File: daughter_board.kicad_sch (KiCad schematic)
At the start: 8 parts

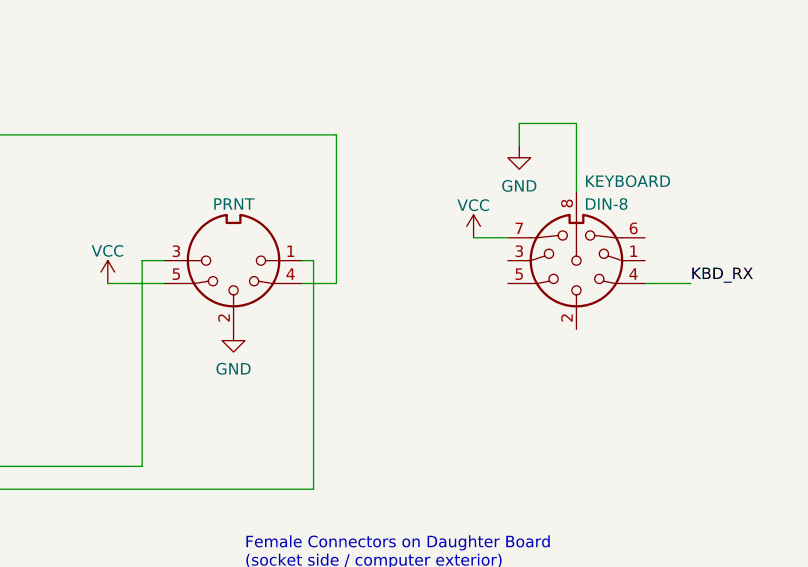
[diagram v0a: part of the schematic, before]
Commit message: Some changes, unfortunately merged with upgrade to kicad v7
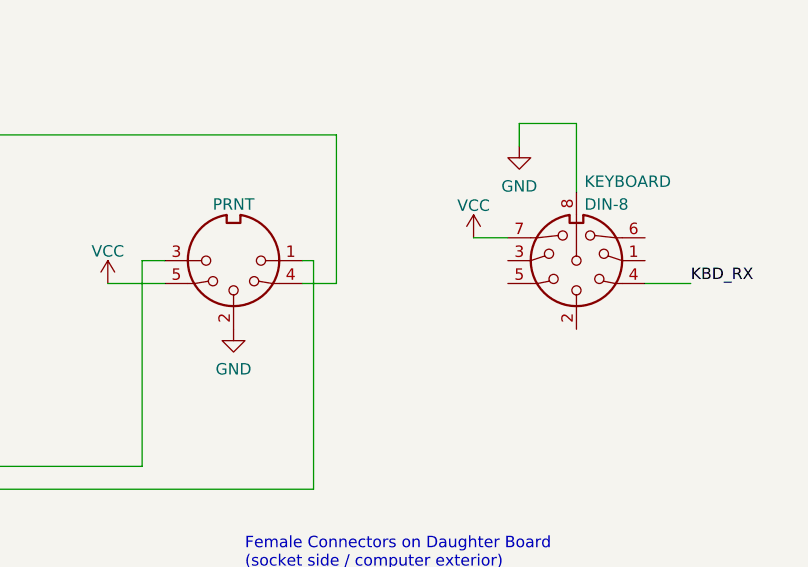
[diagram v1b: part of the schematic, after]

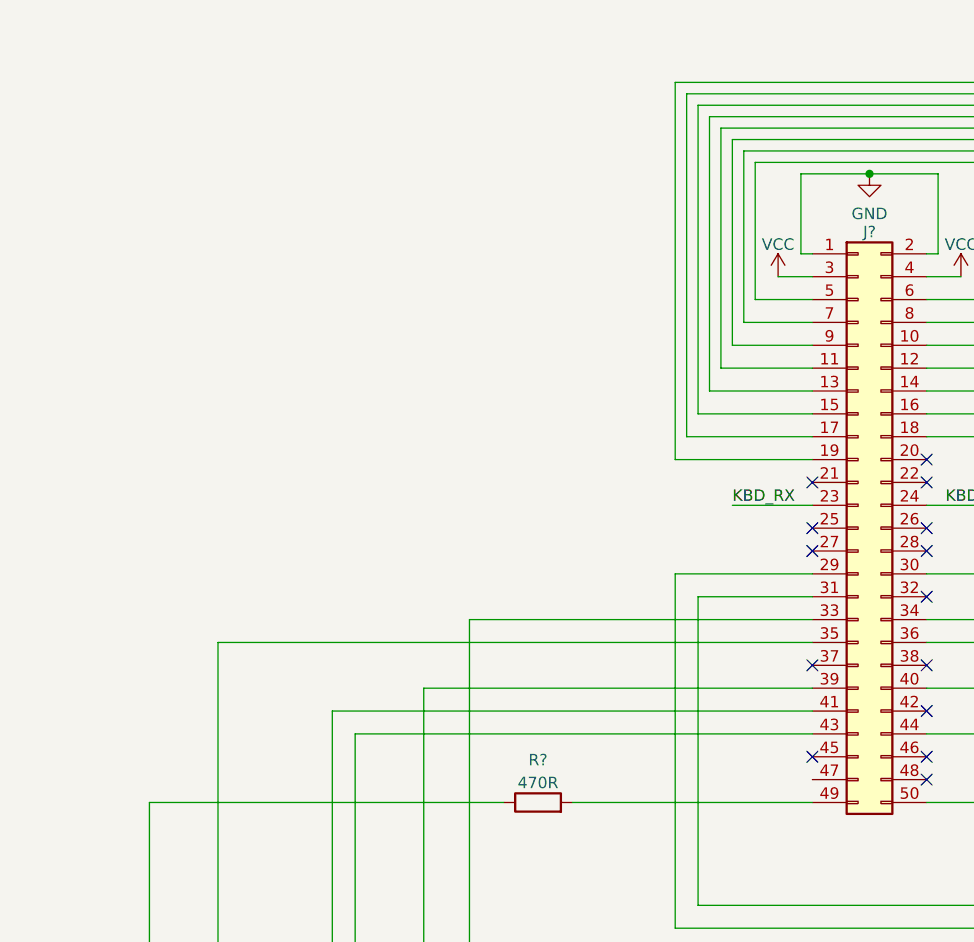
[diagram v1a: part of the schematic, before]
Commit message: Reset circuit
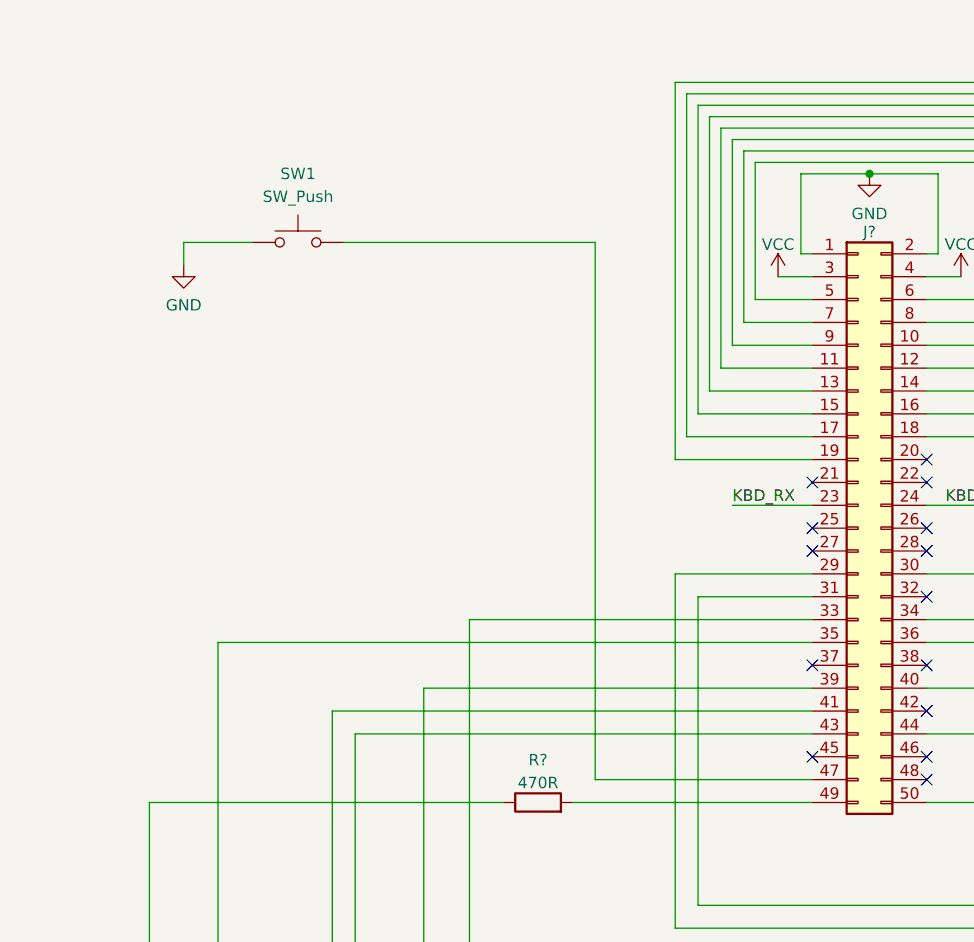
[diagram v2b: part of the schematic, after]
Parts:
- added SW1: SW_Push, symbol Switch:SW_Push
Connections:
- net GND: now also SW1.2
- net at J?.47 (Pin_47): now also SW1.1
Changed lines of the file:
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@@
+    (stroke (width 0) (type default))
+  )
+  (wire (pts (xy 99.06 123.19) (xy 99.06 63.5))
     (stroke (width 0) (type default))
   )
@@
     (stroke (width 0) (type default))
   )
+  (wire (pts (xy 60.96 63.5) (xy 53.34 63.5))
+    (stroke (width 0) (type default))
+  )
   (wire (pts (xy 135.89 125.73) (xy 142.24 125.73))
     (stroke (width 0) (type default))
@@
     (stroke (width 0) (type default))
   )
+  (wire (pts (xy 123.19 123.19) (xy 99.06 123.19))
+    (stroke (width 0) (type default))
+  )
   (wire (pts (xy 57.15 107.95) (xy 57.15 166.37))
     (stroke (width 0) (type default))
@@
     (stroke (width 0) (type default))
   )
+  (wire (pts (xy 71.12 63.5) (xy 99.06 63.5))
+    (stroke (width 0) (type default))
+  )
   (wire (pts (xy 231.14 114.3) (xy 229.87 114.3))
     (stroke (width 0) (type default))
@@
   )
   (wire (pts (xy 107.95 139.7) (xy 231.14 139.7))
+    (stroke (width 0) (type default))
+  )
+  (wire (pts (xy 53.34 63.5) (xy 53.34 66.04))
     (stroke (width 0) (type default))
   )
@@
     )
   )
+  (symbol (lib_id "Switch:SW_Push") (at 66.04 63.5 0) (mirror y) (unit 1)
+    (in_bom yes) (on_board yes) (dnp no) (fields_autoplaced)
+    (property "Reference" "SW1" (at 66.04 55.88 0)
+      (effects (font (size 1.27 1.27)))
+    )
+    (property "Value" "SW_Push" (at 66.04 58.42 0)
+      (effects (font (size 1.27 1.27)))
+    )
+    (property "Footprint" "" (at 66.04 58.42 0)
+      (effects (font (size 1.27 1.27)) hide)
+    )
+    (property "Datasheet" "~" (at 66.04 58.42 0)
+      (effects (font (size 1.27 1.27)) hide)
+    )
+    (pin "1")
+    (pin "2")
+    (instances
+      (project "ceda"
+        (path "/12a6dbe3-008d-4c5b-88f6-9f1c816060be/4f1cc97c-1ae7-488a-96b4-ad54fee0fde4"
+          (reference "SW1") (unit 1)
+        )
+      )
+    )
+  )
   (symbol (lib_id "power:VCC") (at 208.28 116.84 0) (unit 1)
     (in_bom yes) (on_board yes) (dnp no) (fields_autoplaced)
@@
         )
       )
+    )
+  )
+  (symbol (lib_id "power:GND") (at 53.34 66.04 0) (mirror y) (unit 1)
+    (in_bom yes) (on_board yes) (dnp no) (fields_autoplaced)
+    (property "Reference" "#PWR051" (at 53.34 72.39 0)
+      (effects (font (size 1.27 1.27)) hide)
+    )
+    (property "Value" "GND" (at 53.34 70.4834 0)
+      (effects (font (size 1.27 1.27)))
+    )
+    (property "Footprint" "" (at 53.34 66.04 0)
+      (effects (font (size 1.27 1.27)) hide)
+    )
+    (property "Datasheet" "" (at 53.34 66.04 0)
+      (effects (font (size 1.27 1.27)) hide)
+    )
+    (pin "1")
+    (instances
+      (project "ceda"
+        (path "/12a6dbe3-008d-4c5b-88f6-9f1c816060be/4f1cc97c-1ae7-488a-96b4-ad54fee0fde4"
+          (reference "#PWR051") (unit 1)
+        )
+      )

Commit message: Daughterboard
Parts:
- gave numbers to parts that had none: 1
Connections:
- net PRINTER_16: now reaches J2.13 (Pin_13), PRINTER.16 (P16)
- net PRINTER_17: now reaches J2.15 (Pin_15), PRINTER.17 (P17)
- net PRINTER_18: now reaches J2.12 (Pin_12), PRINTER.18 (P18)
- net PRINTER_19: now reaches J2.11 (Pin_11), PRINTER.19 (P19)
- net PRINTER_2: now reaches J2.19 (Pin_19), PRINTER.2
- net PRINTER_20: now reaches J2.10 (Pin_10), PRINTER.20 (P20)
- net PRINTER_21: now reaches J2.9 (Pin_9), PRINTER.21 (P21)
- net PRINTER_22: now reaches J2.8 (Pin_8), PRINTER.22 (P22)
- net PRINTER_23: now reaches J2.7 (Pin_7), PRINTER.23 (P23)
- net PRINTER_24: now reaches J2.6 (Pin_6), PRINTER.24 (P24)
- net PRINTER_25: now reaches J2.5 (Pin_5), PRINTER.25 (P25)
- net PRINTER_3: now reaches J2.14 (Pin_14), PRINTER.3
- net PRINTER_4: now reaches J2.16 (Pin_16), PRINTER.4
- net PRINTER_5: now reaches J2.17 (Pin_17), PRINTER.5
- net PRINTER_9: now reaches J2.18 (Pin_18), PRINTER.9
- net PRNT_1: now reaches J2.29 (Pin_29), PRNT.1
- net PRNT_4: now reaches J2.30 (Pin_30), PRNT.4
- net PRNT_3: now reaches J2.31 (Pin_31), PRNT.3
- net SER_2: now reaches J2.33 (Pin_33), SERIAL.2
- net SER_4: now reaches J2.34 (Pin_34), SERIAL.4
- net SER20: now reaches J2.35 (Pin_35), SERIAL.20 (P20)
- net SER_24: now reaches J2.36 (Pin_36), SCLK.2 (B)
- net SER_3: now reaches J2.39 (Pin_39), SERIAL.3
- net SER_6: now reaches J2.40 (Pin_40), SERIAL.6
- net SER_5: now reaches J2.41 (Pin_41), SERIAL.5
- net SER_17: now reaches J2.43 (Pin_43), SERIAL.17 (P17)
- net SER_15: now reaches J2.44 (Pin_44), SERIAL.15 (P15)
- net ~{RESET_BTN}: now reaches J2.47 (Pin_47), SW1.1
- net SER_9: now reaches J2.49 (Pin_49), R?.2
- net SER_10: now reaches J2.50 (Pin_50), R?.2
- no-connect marks 14 -> 36
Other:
- note added: "This is another board, connected through J2"
- moved on the sheet: J2, KEYBOARD, PRINTER, PRNT, R?, SCLK, SERIAL, SW1

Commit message: VCC -> +5V
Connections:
- net VCC renamed +5V
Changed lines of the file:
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@@
     )
   )
-  (symbol (lib_id "power:VCC") (at 171.45 132.08 90) (unit 1)
-    (in_bom yes) (on_board yes) (dnp no) (fields_autoplaced)
-    (property "Reference" "#PWR0183" (at 175.26 132.08 0)
-      (effects (font (size 1.27 1.27)) hide)
-    )
-    (property "Value" "VCC" (at 170.18 129.54 90)
-      (effects (font (size 1.27 1.27)))
+  (symbol (lib_id "power:+5V") (at 171.45 132.08 90) (unit 1)
+    (in_bom yes) (on_board yes) (dnp no) (fields_autoplaced)
+    (property "Reference" "#PWR?" (at 175.26 132.08 0)
+      (effects (font (size 1.27 1.27)) hide)
+    )
+    (property "Value" "+5V" (at 167.64 132.08 90)
+      (effects (font (size 1.27 1.27)) (justify left))
     )
     (property "Footprint" "" (at 171.45 132.08 0)
@@
       (project "ceda"
         (path "/12a6dbe3-008d-4c5b-88f6-9f1c816060be/4f1cc97c-1ae7-488a-96b4-ad54fee0fde4"
-          (reference "#PWR0183") (unit 1)
+          (reference "#PWR?") (unit 1)
         )
       )
@@
     )
   )
-  (symbol (lib_id "power:VCC") (at 40.64 71.12 0) (unit 1)
-    (in_bom yes) (on_board yes) (dnp no) (fields_autoplaced)
-    (property "Reference" "#PWR0185" (at 40.64 74.93 0)
-      (effects (font (size 1.27 1.27)) hide)
-    )
-    (property "Value" "VCC" (at 40.64 67.5442 0)
+  (symbol (lib_id "power:+5V") (at 40.64 71.12 0) (unit 1)
+    (in_bom yes) (on_board yes) (dnp no) (fields_autoplaced)
+    (property "Reference" "#PWR?" (at 40.64 74.93 0)
+      (effects (font (size 1.27 1.27)) hide)
+    )
+    (property "Value" "+5V" (at 40.64 66.04 0)
       (effects (font (size 1.27 1.27)))
     )
@@
       (project "ceda"
         (path "/12a6dbe3-008d-4c5b-88f6-9f1c816060be/4f1cc97c-1ae7-488a-96b4-ad54fee0fde4"
-          (reference "#PWR0185") (unit 1)
+          (reference "#PWR?") (unit 1)
         )
       )
@@
     )
   )
-  (symbol (lib_id "power:VCC") (at 229.87 127 0) (unit 1)
+  (symbol (lib_id "power:+5V") (at 229.87 127 0) (unit 1)
     (in_bom yes) (on_board yes) (dnp no)
-    (property "Reference" "#PWR0178" (at 229.87 130.81 0)
-      (effects (font (size 1.27 1.27)) hide)
-    )
-    (property "Value" "VCC" (at 229.87 123.4242 0)
+    (property "Reference" "#PWR?" (at 229.87 130.81 0)
+      (effects (font (size 1.27 1.27)) hide)
+    )
+    (property "Value" "+5V" (at 229.87 123.444 0)
       (effects (font (size 1.27 1.27)))
     )
@@
       (project "ceda"
         (path "/12a6dbe3-008d-4c5b-88f6-9f1c816060be/4f1cc97c-1ae7-488a-96b4-ad54fee0fde4"
-          (reference "#PWR0178") (unit 1)
+          (reference "#PWR?") (unit 1)
         )
       )
@@
     )
   )
-  (symbol (lib_id "power:VCC") (at 156.21 26.67 90) (unit 1)
-    (in_bom yes) (on_board yes) (dnp no) (fields_autoplaced)
-    (property "Reference" "#PWR0179" (at 160.02 26.67 0)
-      (effects (font (size 1.27 1.27)) hide)
-    )
-    (property "Value" "VCC" (at 154.94 24.13 90)
-      (effects (font (size 1.27 1.27)))
+  (symbol (lib_id "power:+5V") (at 156.21 26.67 90) (unit 1)
+    (in_bom yes) (on_board yes) (dnp no) (fields_autoplaced)
+    (property "Reference" "#PWR?" (at 160.02 26.67 0)
+      (effects (font (size 1.27 1.27)) hide)
+    )
+    (property "Value" "+5V" (at 152.4 26.67 90)
+      (effects (font (size 1.27 1.27)) (justify left))
     )
     (property "Footprint" "" (at 156.21 26.67 0)
@@
       (project "ceda"
         (path "/12a6dbe3-008d-4c5b-88f6-9f1c816060be/4f1cc97c-1ae7-488a-96b4-ad54fee0fde4"
-          (reference "#PWR0179") (unit 1)
+          (reference "#PWR?") (unit 1)
         )
       )
@@
     )
   )
-  (symbol (lib_id "power:VCC") (at 60.96 71.12 0) (unit 1)
-    (in_bom yes) (on_board yes) (dnp no) (fields_autoplaced)
-    (property "Reference" "#PWR0181" (at 60.96 74.93 0)
-      (effects (font (size 1.27 1.27)) hide)
-    )
-    (property "Value" "VCC" (at 60.96 67.5442 0)
+  (symbol (lib_id "power:+5V") (at 60.96 71.12 0) (unit 1)
+    (in_bom yes) (on_board yes) (dnp no) (fields_autoplaced)
+    (property "Reference" "#PWR?" (at 60.96 74.93 0)
+      (effects (font (size 1.27 1.27)) hide)
+    )
+    (property "Value" "+5V" (at 60.96 66.04 0)
       (effects (font (size 1.27 1.27)))
     )
@@
       (project "ceda"
         (path "/12a6dbe3-008d-4c5b-88f6-9f1c816060be/4f1cc97c-1ae7-488a-96b4-ad54fee0fde4"
-          (reference "#PWR0181") (unit 1)
-        )
-      )
+          (reference "#PWR?") (unit 1)
+        )
+      )

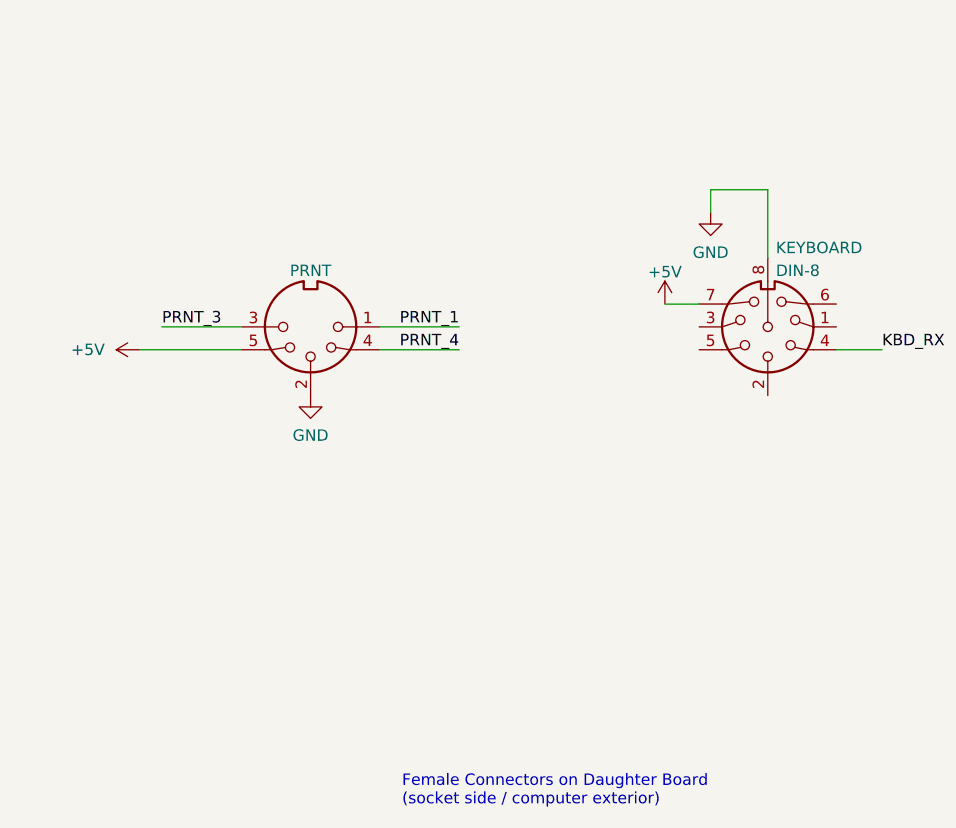
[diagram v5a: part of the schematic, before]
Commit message: Notes in kicad's sheet text blocks
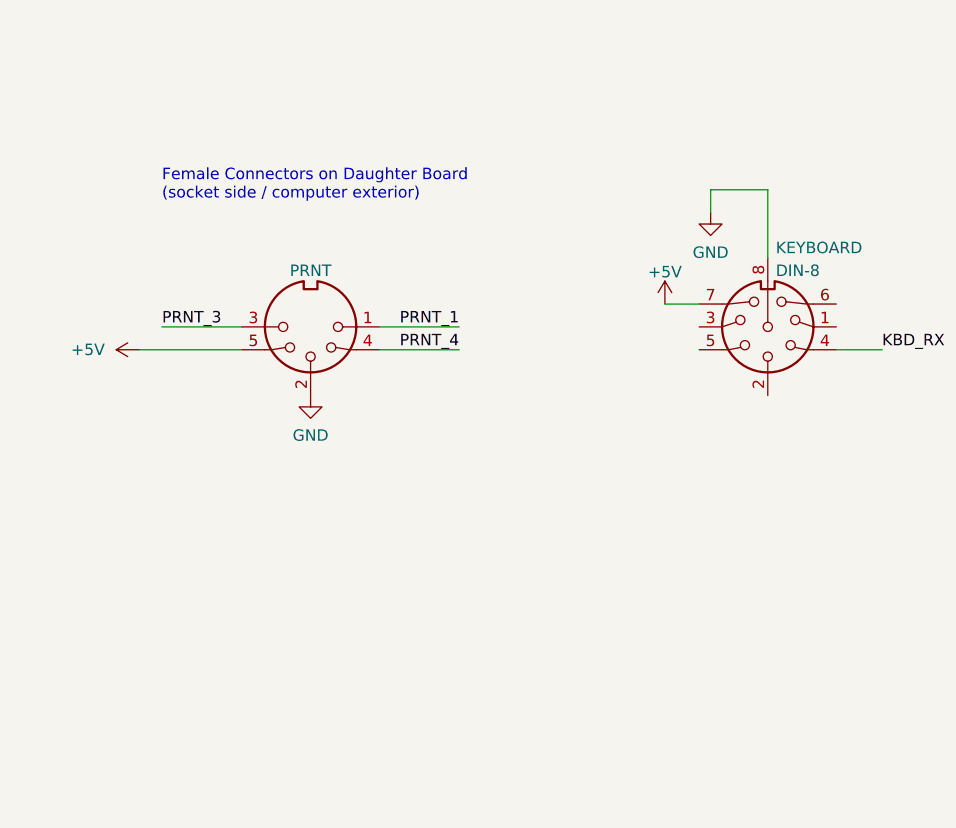
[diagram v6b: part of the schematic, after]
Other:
- company: (none) -> Logic Systems Int'l Inc
- title: Daughter Board -> CEDA - Sanco 8003 schematics
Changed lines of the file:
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@@
   (paper "A4")
   (title_block
-    (title "Daughter Board")
+    (title "CEDA - Sanco 8003 schematics")
     (date "2023-02-26")
+    (rev "05")
+    (company "Logic Systems Int'l Inc")
+    (comment 1 "reversed by RetrOfficina - retrofficina.glgprograms.it")
+    (comment 3 "I/O interface to the peripherals")
+    (comment 4 "Daughterboard")
   )
   (junction (at 50.8 59.69) (diameter 0) (color 0 0 0 0)
@@
   )
   (text "Female Connectors on Daughter Board\n(socket side / computer exterior)"
-    (at 200.66 182.88 0)
+    (at 173.99 115.57 0)
     (effects (font (size 1.27 1.27)) (justify left bottom))
   )

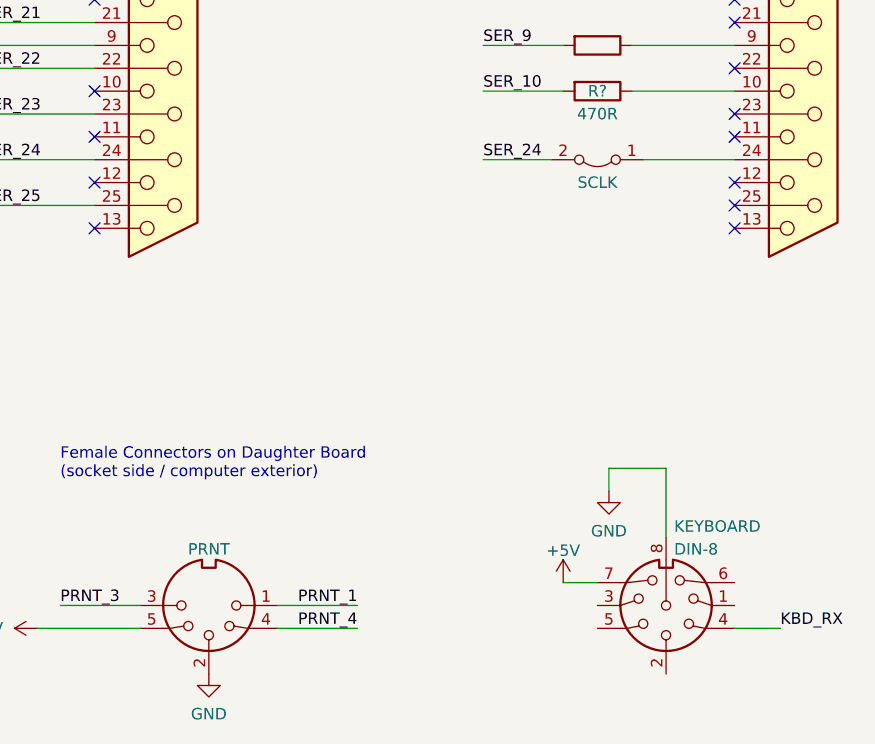
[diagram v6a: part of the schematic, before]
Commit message: Upgrade to KiCAD 9.0
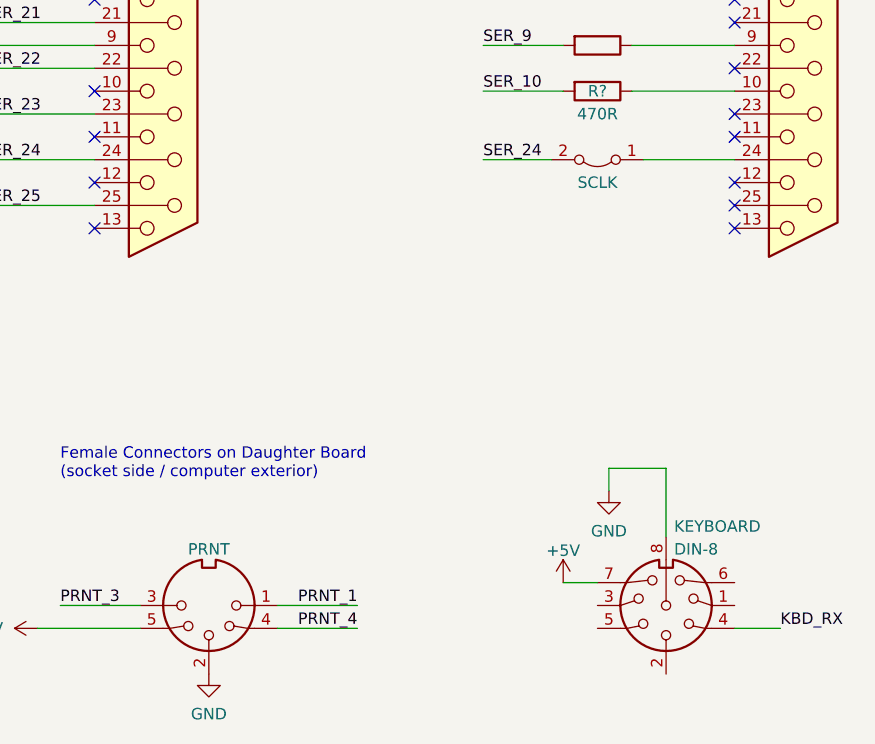
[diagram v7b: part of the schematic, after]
